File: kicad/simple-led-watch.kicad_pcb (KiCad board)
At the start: 4 copper layers, 32.8 x 32.6 mm, 167 parts, among them P1 BATTERY, P3 USB_OTG, Q1 MMBT3904, Q2 MMBT3904, SW1 SPST-4PIN, SW2 SPST-4PIN, SW3 SPST-4PIN, SW4 SPST-4PIN, U1 MCP73832, U2 TPS62736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

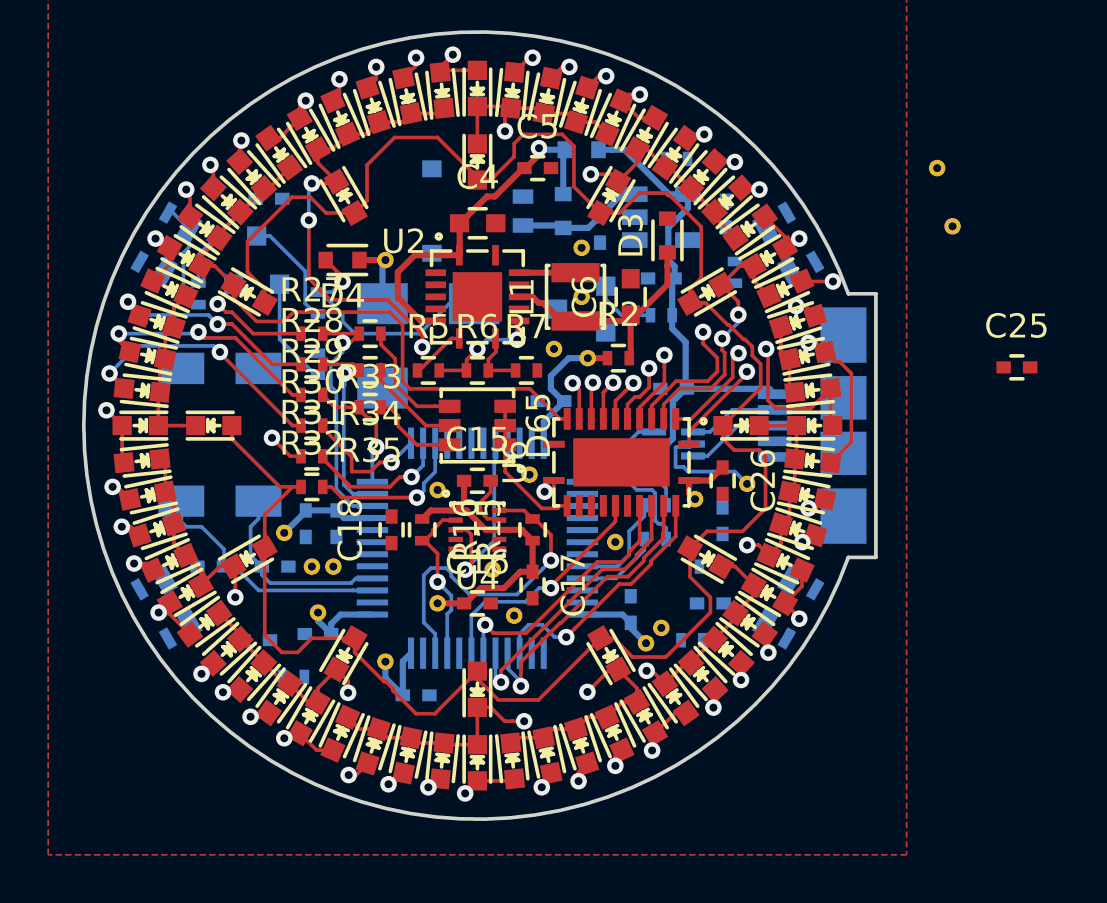
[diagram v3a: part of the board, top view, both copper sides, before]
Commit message: Selected programming header
Only one non-connected trace left. And I don't know where it is...
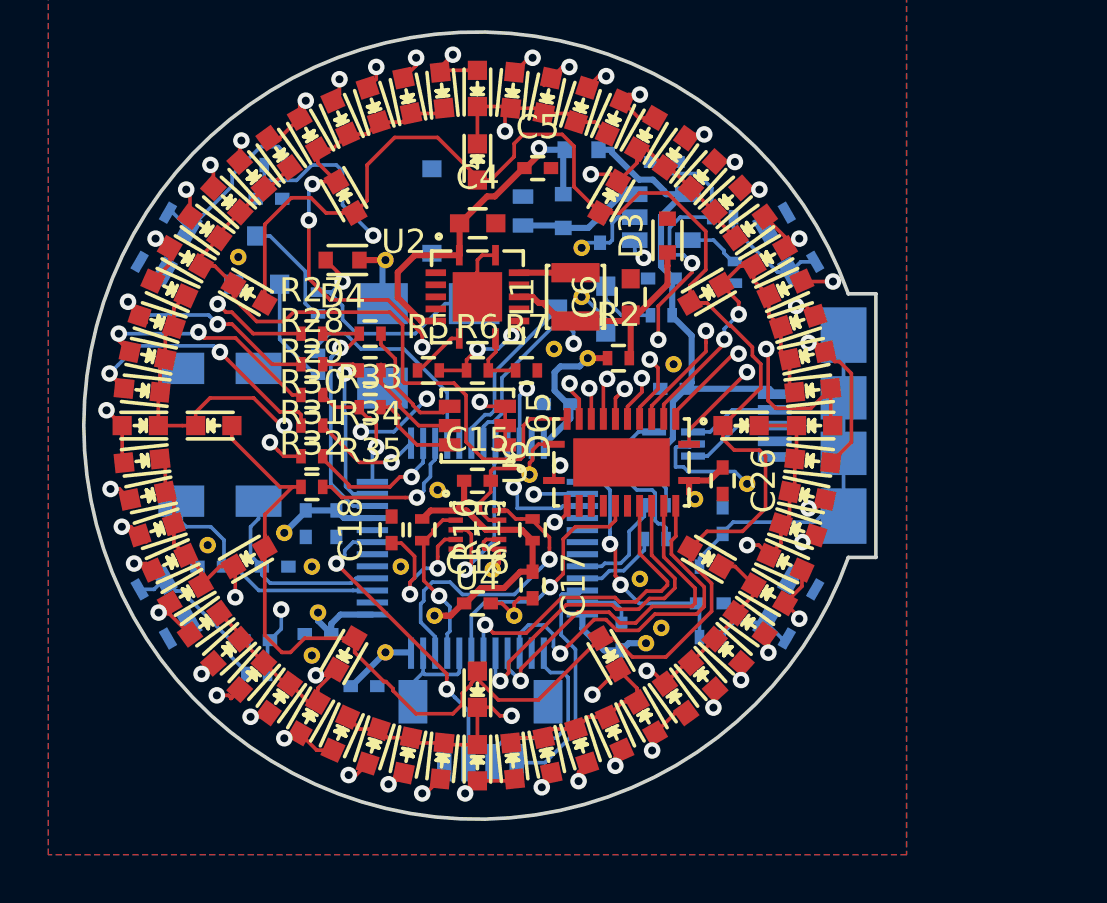
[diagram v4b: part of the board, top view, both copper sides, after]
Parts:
- removed C25: 1u, Capacitors_SMD:C_0402
- removed the REF** at (159.1, 94.7)
- removed the REF** at (184.8, 80.6)
- removed the REF** at (184.2, 78.2)
- added P2: SWD, simple-led-watch:JST-SH-4, B.Cu at (165.2, 99.4)
- added REF**: 1PIN_VIA, simple-led-watch:1PIN_VIA, F.Cu at (173.2, 86.4)
- added REF**: 1PIN_VIA, simple-led-watch:1PIN_VIA, F.Cu at (161.9, 94.7)
- added REF**: 1PIN_VIA, simple-led-watch:1PIN_VIA, F.Cu at (153.9, 93.9)
- added REF**: 1PIN_VIA, simple-led-watch:1PIN_VIA, F.Cu at (158.2, 98.4)
- added REF**: 1PIN_VIA, simple-led-watch:1PIN_VIA, F.Cu at (155.2, 81.9)
- moved R26 6.21 mm to (156.7, 78.1), turned to 0 degrees
- moved C19 3.33 mm to (172.8, 78.0), turned to 0 degrees
- moved R20 3.07 mm to (175.3, 80.3), turned to 0 degrees
- moved C10 2.19 mm to (160.4, 99.7)
- moved REF** 1.83 mm to (171.8, 95.2)
- moved R24 1.53 mm to (156.0, 99.2)
- moved C8 1.20 mm to (171.1, 97.7)
- moved R22 0.77 mm to (174.8, 97.7)
- moved REF** 0.52 mm to (163.3, 96.8)
- moved REF** 0.38 mm to (161.3, 98.3)
- moved C7 0.28 mm to (168.4, 88.0)
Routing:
- net GND: track 7.21 -> 38.6 mm
- net /Control/BTN2: track 0.00 -> 27.0 mm, vias 0 -> 2
- net /Control/BTN3: track 4.50 -> 28.8 mm, vias 0 -> 2
- net /Control/BTN0: track 0.00 -> 20.8 mm, vias 0 -> 3
- net /LEDs/LED_SEG9: track 9.00 -> 28.2 mm, vias 1 -> 4
- net /Control/CHG_STAT: track 0.00 -> 14.7 mm, vias 0 -> 2
- net /USB/USB_SHIELD: track 0.00 -> 14.6 mm
- net /Control/STM32_RESET: track 0.00 -> 12.5 mm, vias 0 -> 2
- net /Control/BTN1: track 0.00 -> 10.3 mm, vias 0 -> 2
- net /Control/SWDIO: track 0.00 -> 9.84 mm
- net /Control/BUZ_OUTPUT: track 0.00 -> 9.01 mm
- net /Control/SWCLK: track 0.00 -> 7.78 mm
- net /Control/~USB_PRES: track 0.00 -> 7.16 mm
- net Net-(R24-Pad2): track 0.00 -> 6.65 mm
- net Net-(C18-Pad1): track 0.00 -> 6.47 mm, vias 0 -> 2
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
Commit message: Placed parts for round two
I'm pretty sure I can do it better
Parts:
- removed the REF** at (173.2, 86.4)
- removed the REF** at (165.7, 94.9)
- removed the REF** at (169.4, 81.5)
- removed the REF** at (169.4, 83.6)
- removed the REF** at (168.3, 85.7)
- removed the REF** at (176.3, 91.3)
- removed the REF** at (167.3, 90.9)
- removed the REF** at (158.2, 94.7)
- removed the REF** at (169.7, 86.1)
- removed the REF** at (172.1, 97.9)
- removed the REF** at (161.3, 98.3)
- removed the REF** at (166.6, 96.8)
- removed the REF** at (158.5, 96.6)
- removed the REF** at (163.3, 96.8)
- removed the REF** at (157.1, 93.3)
- removed the REF** at (174.1, 91.9)
- removed the REF** at (161.3, 82.0)
- removed the REF** at (161.9, 94.7)
- removed the REF** at (153.9, 93.9)
- removed the REF** at (158.2, 98.4)
- removed the REF** at (155.2, 81.9)
- removed the REF** at (172.7, 97.3)
- removed the REF** at (171.8, 95.2)
- removed the REF** at (163.4, 91.6)
- added C25: 1u, Capacitors_SMD:C_0402, F.Cu at (162.7, 98.0)
- added REF**: 1PIN_VIA, simple-led-watch:1PIN_VIA, F.Cu at (167.3, 82.2)
- added REF**: 1PIN_VIA, simple-led-watch:1PIN_VIA, F.Cu at (166.2, 82.2)
- added REF**: 1PIN_VIA, simple-led-watch:1PIN_VIA, F.Cu at (166.2, 81.2)
- added REF**: 1PIN_VIA, simple-led-watch:1PIN_VIA, F.Cu at (167.3, 81.2)
- C10, C11, C12, C7, C8, C9, D1, D2, Q1, R1, R4: moved to F.Cu
- U6: moved to B.Cu
- moved C10 18.9 mm to (170.3, 83.6), turned to 90 degrees
- moved C26 13.8 mm to (162.7, 96.8), turned to 180 degrees
- moved U6 11.4 mm to (162.1, 97.4)
- moved C6 10.8 mm to (160.7, 82.5), turned to 270 degrees
- moved R2 10.3 mm to (162.6, 80.1)
- moved D1 10.0 mm to (169.8, 87.5)
- moved R5 9.80 mm to (168.1, 78.2), turned to 90 degrees
- moved C12 9.12 mm to (163.7, 85.9)
- moved R6 8.54 mm to (163.4, 78.2), turned to 270 degrees
- moved R7 8.39 mm to (166.8, 78.2), turned to 90 degrees
- moved C5 8.17 mm to (166.8, 86.4), turned to 180 degrees
- moved C8 7.82 mm to (169.3, 90.0)
- moved C11 7.79 mm to (162.4, 85.9)
- moved C22 7.18 mm to (151.4, 84.6)
- moved Q1 7.17 mm to (172.2, 90.7), turned to 90 degrees
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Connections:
- P2 pad NC: GND -> (no net)
- Y1 pad 1: /Control/STM32_OSC32- -> /Control/STM32_OSC32+
- Y1 pad 2: /Control/STM32_OSC32+ -> /Control/STM32_OSC32-
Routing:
- net /LEDs/LED_A_R2: track 113.5 -> 0.00 mm, vias 13 -> 0
- net /LEDs/LED_A_R1: track 110.3 -> 0.00 mm, vias 13 -> 0
- net /LEDs/LED_A_R3: track 109.9 -> 0.00 mm, vias 12 -> 0
- net /LEDs/LED_A_R0: track 104.0 -> 0.00 mm, vias 7 -> 0
- net /LEDs/LED_A_R4: track 103.3 -> 0.00 mm, vias 7 -> 0
- net /LEDs/LED_A_R5: track 87.4 -> 0.00 mm
- net /LEDs/LED_SEG8: track 39.0 -> 0.00 mm, vias 2 -> 0
- net +3V3: track 38.7 -> 0.00 mm
- net GND: track 38.6 -> 0.00 mm
- net /LEDs/LED_SEG7: track 36.6 -> 0.00 mm, vias 2 -> 0
- net /LEDs/LED_SEG11: track 30.9 -> 0.00 mm, vias 4 -> 0
- net /LEDs/LED_SEG0: track 30.6 -> 0.00 mm, vias 2 -> 0
- net /LEDs/LED_SEG10: track 28.8 -> 0.00 mm
- net /Control/BTN3: track 28.8 -> 0.00 mm, vias 2 -> 0
- net /LEDs/LED_SEG9: track 28.2 -> 0.00 mm, vias 4 -> 0
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- removed copper zone on In1.Cu, net +3V3
- removed copper zone on B.Cu, net GND
- removed copper zone on F.Cu, net GND
- removed copper zone on In2.Cu, net GND

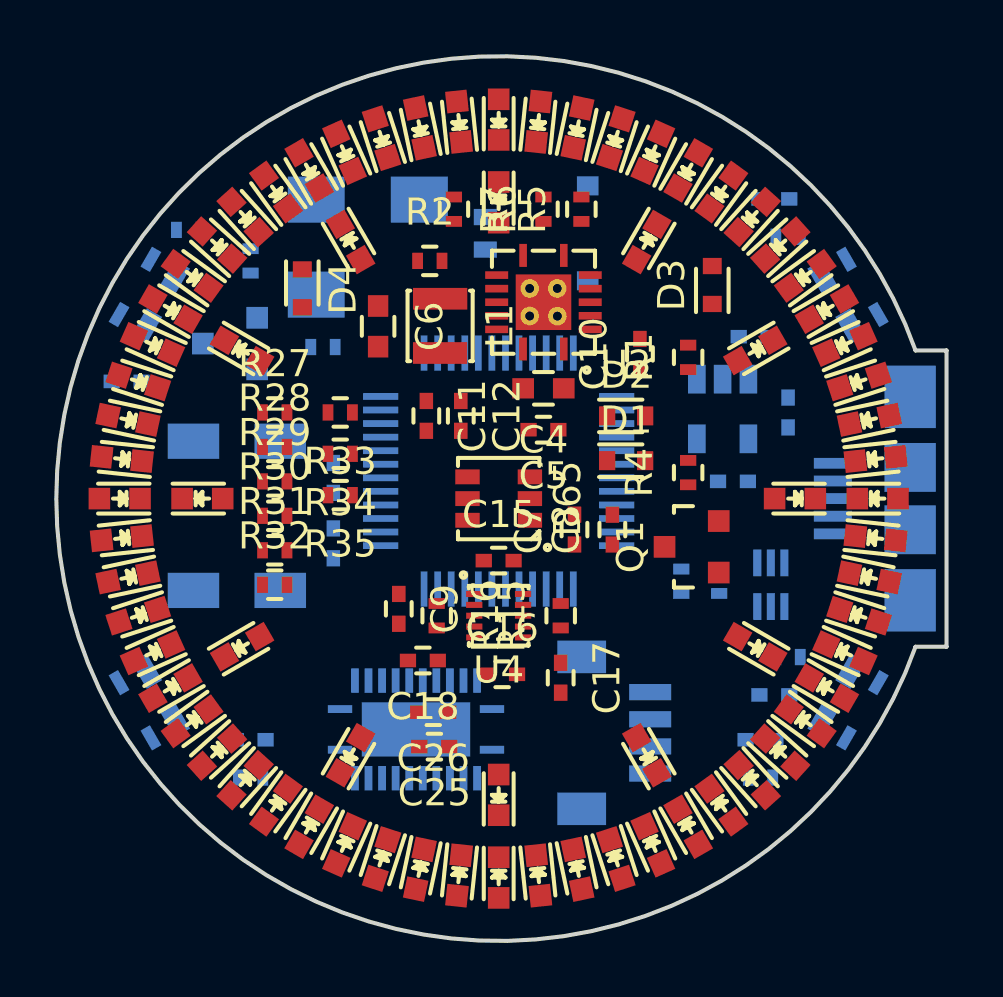
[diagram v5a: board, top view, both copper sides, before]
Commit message: Finished round two routing
This layout cuts through the middle of no planes and has more
predictable power paths (without needing Hyperlynx or something like
that). It also routes all signals but the LED-related ones on just the
top and bottom layers, as it is meant to be. It also nearly comforms to
the recommended layout for the regulator. There also aren't any ICs
without a full reference plane beneath them.

Basically, it's awesome.
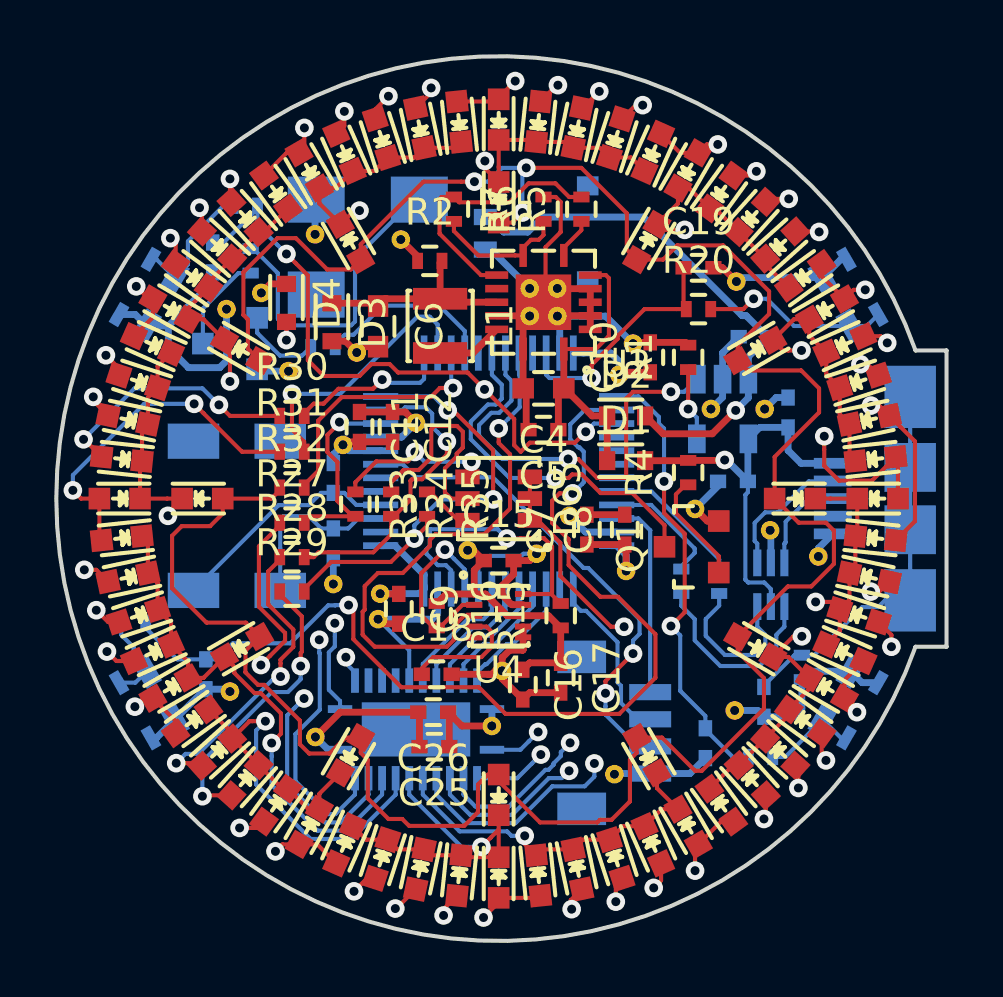
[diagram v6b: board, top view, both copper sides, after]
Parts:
- added REF**: 1PIN_VIA, simple-led-watch:1PIN_VIA, F.Cu at (156.3, 81.3)
- added REF**: 1PIN_VIA, simple-led-watch:1PIN_VIA, F.Cu at (159.9, 83.5)
- added REF**: 1PIN_VIA, simple-led-watch:1PIN_VIA, F.Cu at (169.4, 99.1)
- added REF**: 1PIN_VIA, simple-led-watch:1PIN_VIA, F.Cu at (167.7, 89.5)
- added REF**: 1PIN_VIA, simple-led-watch:1PIN_VIA, F.Cu at (174.9, 85.6)
- added REF**: 1PIN_VIA, simple-led-watch:1PIN_VIA, F.Cu at (172.9, 85.6)
- added REF**: 1PIN_VIA, simple-led-watch:1PIN_VIA, F.Cu at (169.8, 91.6)
- added REF**: 1PIN_VIA, simple-led-watch:1PIN_VIA, F.Cu at (166.5, 90.9)
- added REF**: 1PIN_VIA, simple-led-watch:1PIN_VIA, F.Cu at (165.2, 95.2)
- added REF**: 1PIN_VIA, simple-led-watch:1PIN_VIA, F.Cu at (160.7, 93.3)
- added REF**: 1PIN_VIA, simple-led-watch:1PIN_VIA, F.Cu at (164.0, 90.8)
- added REF**: 1PIN_VIA, simple-led-watch:1PIN_VIA, F.Cu at (173.8, 96.7)
- added REF**: 1PIN_VIA, simple-led-watch:1PIN_VIA, F.Cu at (160.7, 92.4)
- added REF**: 1PIN_VIA, simple-led-watch:1PIN_VIA, F.Cu at (159.0, 92.0)
- added REF**: 1PIN_VIA, simple-led-watch:1PIN_VIA, F.Cu at (159.4, 86.9)
- added REF**: 1PIN_VIA, simple-led-watch:1PIN_VIA, F.Cu at (162.1, 86.1)
- added REF**: 1PIN_VIA, simple-led-watch:1PIN_VIA, F.Cu at (170.1, 83.2)
- added REF**: 1PIN_VIA, simple-led-watch:1PIN_VIA, F.Cu at (169.5, 84.3)
- added REF**: 1PIN_VIA, simple-led-watch:1PIN_VIA, F.Cu at (176.9, 91.0)
- added REF**: 1PIN_VIA, simple-led-watch:1PIN_VIA, F.Cu at (175.1, 90.1)
- added REF**: 1PIN_VIA, simple-led-watch:1PIN_VIA, F.Cu at (172.3, 89.3)
- added REF**: 1PIN_VIA, simple-led-watch:1PIN_VIA, F.Cu at (161.5, 79.3)
- added REF**: 1PIN_VIA, simple-led-watch:1PIN_VIA, F.Cu at (173.9, 80.9)
- added REF**: 1PIN_VIA, simple-led-watch:1PIN_VIA, F.Cu at (155.2, 96.0)
- added REF**: 1PIN_VIA, simple-led-watch:1PIN_VIA, F.Cu at (158.3, 79.2)
- added REF**: 1PIN_VIA, simple-led-watch:1PIN_VIA, F.Cu at (155.1, 81.9)
- added REF**: 1PIN_VIA, simple-led-watch:1PIN_VIA, F.Cu at (164.8, 97.3)
- added REF**: 1PIN_VIA, simple-led-watch:1PIN_VIA, F.Cu at (158.3, 97.7)
- added REF**: 1PIN_VIA, simple-led-watch:1PIN_VIA, F.Cu at (157.4, 84.2)
- C19, R20: moved to F.Cu
- moved D3 14.1 mm to (159.0, 82.4), turned to 270 degrees
- moved R24 7.16 mm to (151.6, 93.5)
- moved C22 5.57 mm to (154.6, 80.0), turned to 270 degrees
- moved R20 4.24 mm to (172.5, 81.9)
- moved R27 4.11 mm to (157.5, 89.8)
- moved R28 4.11 mm to (157.5, 91.1)
- moved R29 4.11 mm to (157.5, 92.3)
- moved C19 3.78 mm to (172.5, 80.4)
- moved R30 3.74 mm to (157.5, 85.9)
- moved R31 3.69 mm to (157.5, 87.2)
- moved R32 3.64 mm to (157.5, 88.5)
- moved R33 3.42 mm to (159.8, 89.1), turned to 270 degrees
- moved R35 3.22 mm to (162.5, 89.1), turned to 270 degrees
- moved C21 2.92 mm to (154.3, 95.4), turned to 270 degrees
- moved R34 2.64 mm to (161.1, 89.1), turned to 270 degrees
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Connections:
- U6 pad 18: /Control/~LED_C_EN -> GND
- U6 pad 19: GND -> /Control/~LED_C_EN
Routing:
- net /LEDs/LED_A_R2: track 0.00 -> 113.5 mm, vias 0 -> 13
- net /LEDs/LED_A_R1: track 0.00 -> 112.0 mm, vias 0 -> 13
- net /LEDs/LED_A_R0: track 0.00 -> 108.5 mm, vias 0 -> 7
- net /LEDs/LED_A_R3: track 0.00 -> 107.1 mm, vias 0 -> 12
- net /LEDs/LED_A_R4: track 0.00 -> 106.7 mm, vias 0 -> 7
- net GND: track 0.00 -> 100.3 mm
- net /LEDs/LED_A_R5: track 0.00 -> 96.8 mm, vias 0 -> 3
- net /LEDs/LED_SEG0: track 0.00 -> 49.0 mm, vias 0 -> 2
- net /LEDs/LED_SEG1: track 0.00 -> 41.5 mm, vias 0 -> 2
- net /Control/BTN2: track 0.00 -> 37.4 mm, vias 0 -> 2
- net /LEDs/LED_SEG10: track 0.00 -> 37.2 mm, vias 0 -> 2
- net /LEDs/LED_SEG11: track 0.00 -> 36.8 mm, vias 0 -> 2
- net /LEDs/LED_SEG2: track 0.00 -> 36.4 mm, vias 0 -> 2
- net +3V3: track 0.00 -> 33.4 mm
- net /LEDs/LED_RGB_C: track 0.00 -> 28.5 mm, vias 0 -> 2
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- added copper zone on In1.Cu, net +3V3
- added copper zone on In2.Cu, net GND

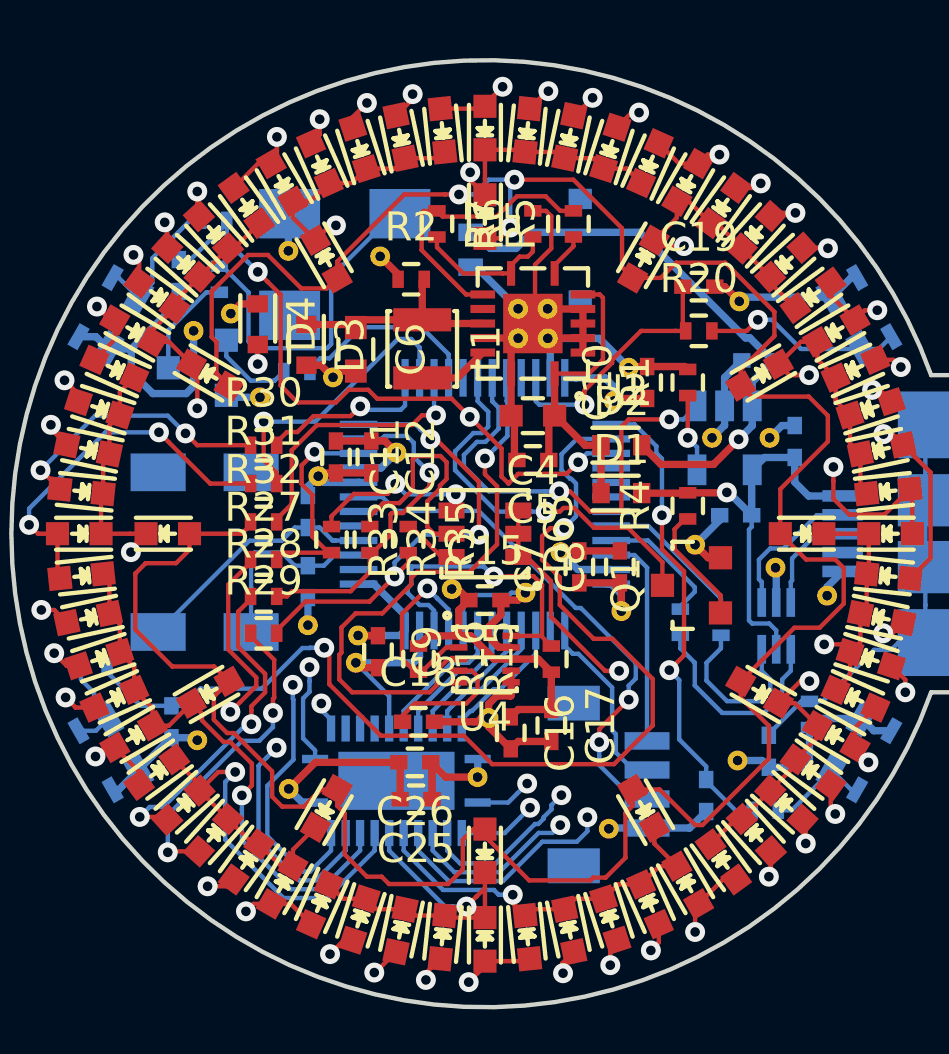
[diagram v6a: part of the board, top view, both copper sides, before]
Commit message: Fixed silkscreen and added markings
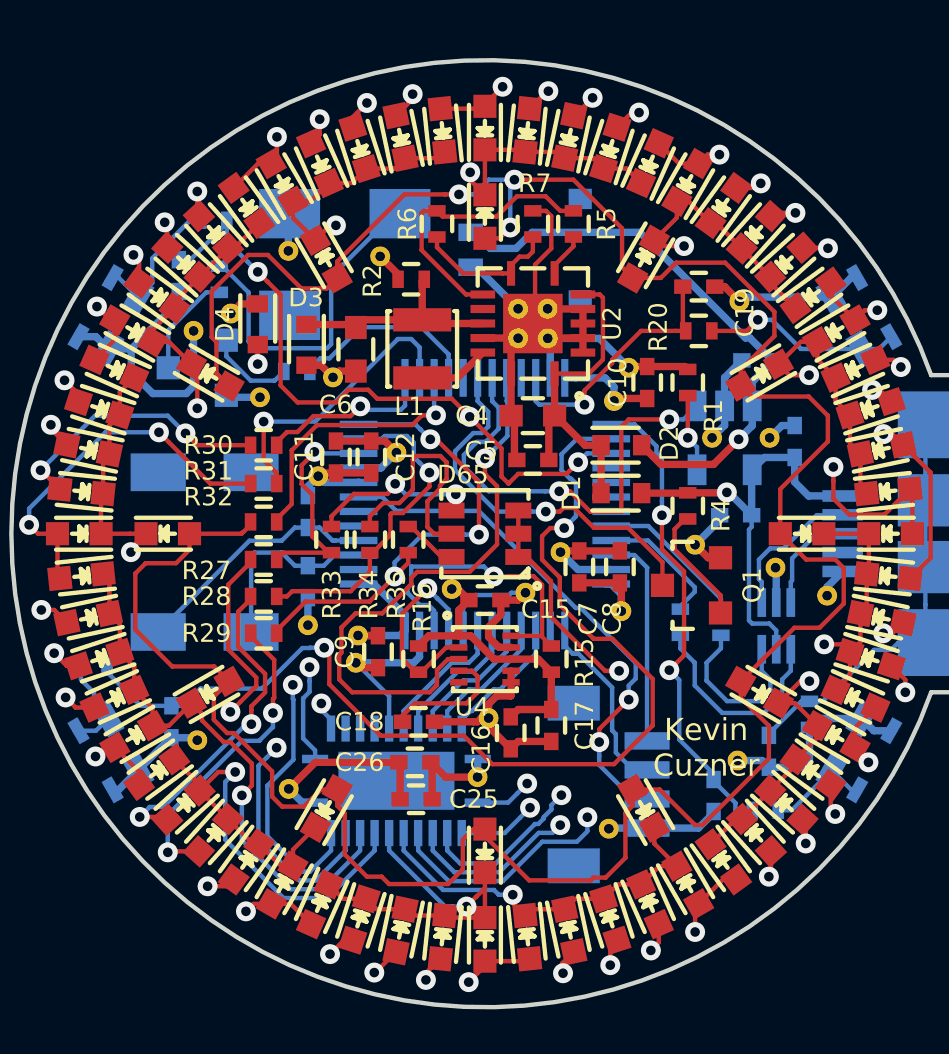
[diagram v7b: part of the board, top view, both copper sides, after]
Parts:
- moved C20 0.25 mm to (173.0, 97.9)
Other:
- board text added: "+"
- board text added: "-"
- board text added: "2016"
- board text added: "3.7V Li-Ion/Li-Poly"
- board text added: "D C R G"
- board text added: "Kevin Cuzner"
- board text added: "LED Watch"
- board text added: "Rev. A"
- board text added: "SWD"
